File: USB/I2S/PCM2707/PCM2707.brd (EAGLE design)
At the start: 43.2 x 38.1 mm, 16 parts, among them J1 J7MM, J2 J7MM, J3 J7MM, Q1 12MHz

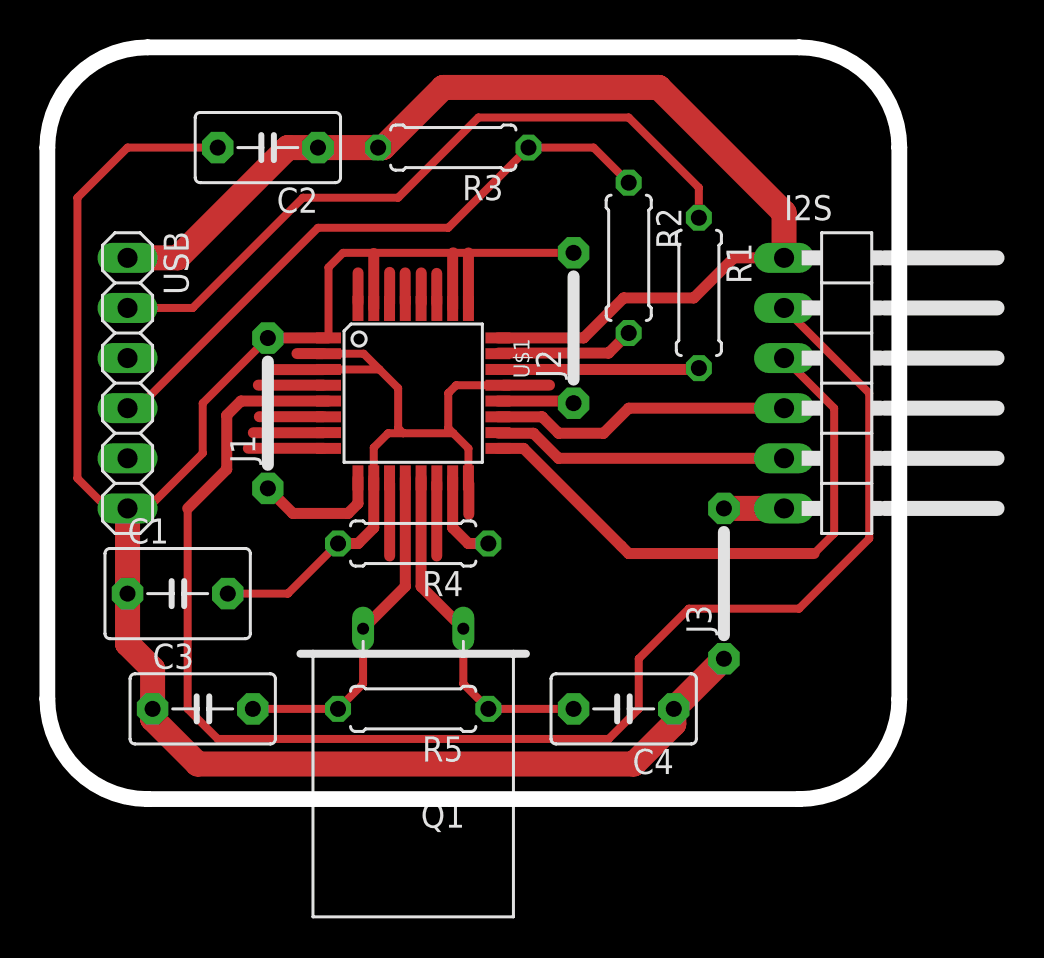
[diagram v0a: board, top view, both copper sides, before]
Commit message: Wire width change
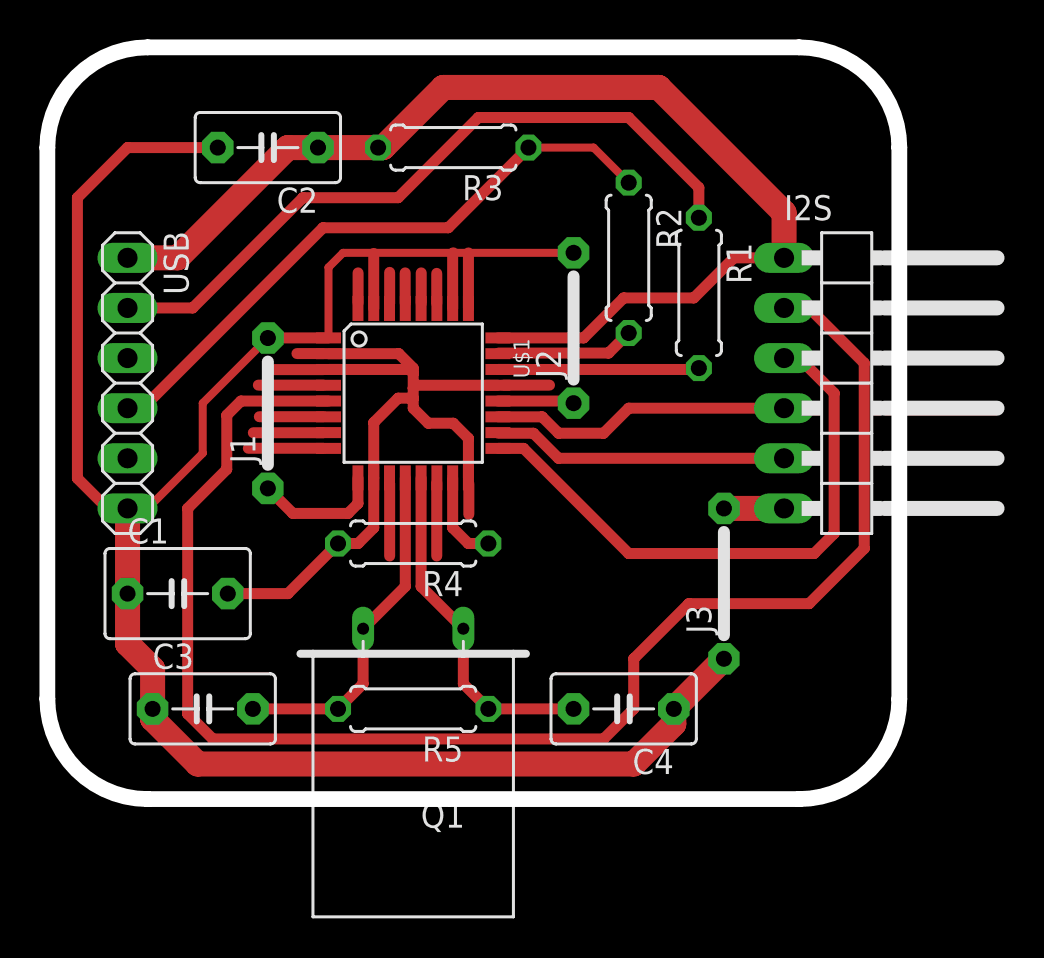
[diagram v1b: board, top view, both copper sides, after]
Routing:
- net N$1: track 33.8 -> 37.4 mm
- net GND: track 122.9 -> 121.9 mm
- net LRCK: track 75.5 -> 76.3 mm
